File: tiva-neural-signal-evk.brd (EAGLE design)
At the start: 100 x 80 mm, 9 parts, among them IC1 TM4C123G, IC2 TLV70233, X1 USB

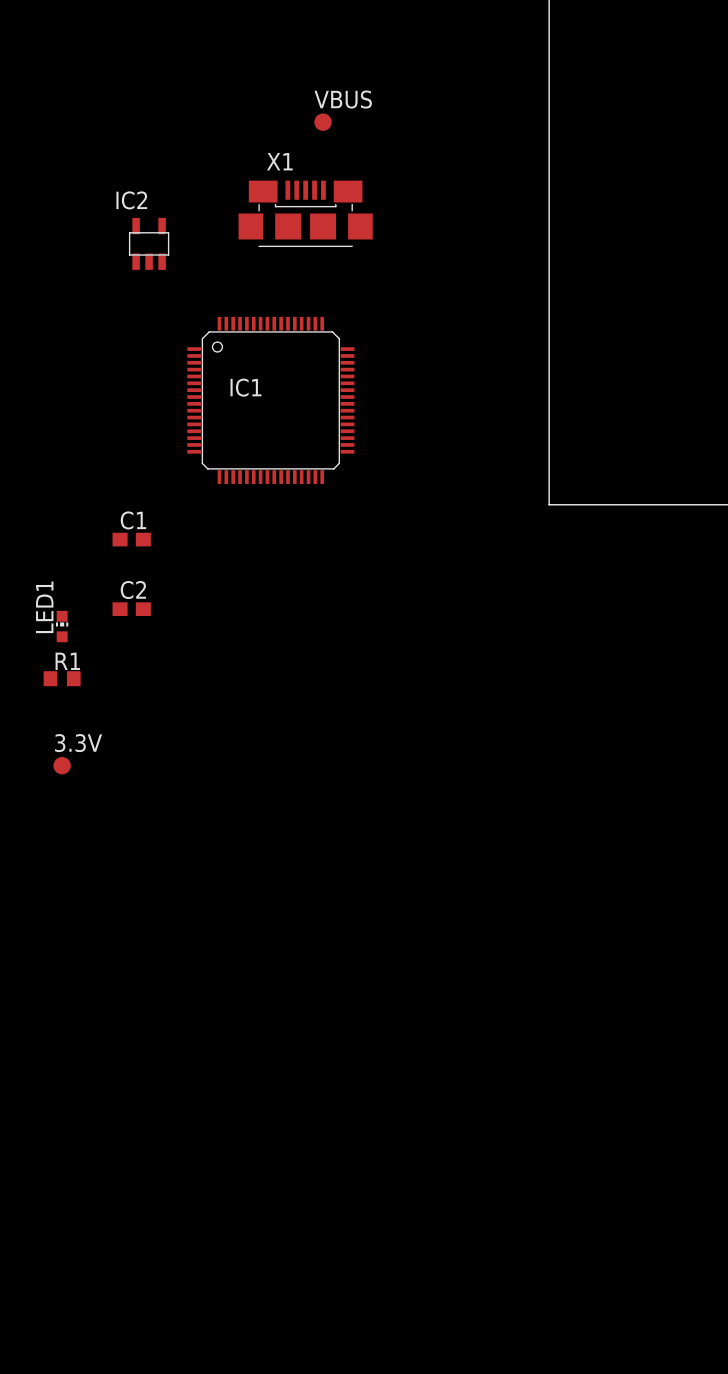
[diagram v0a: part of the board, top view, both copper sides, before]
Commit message: added MCU power circuit
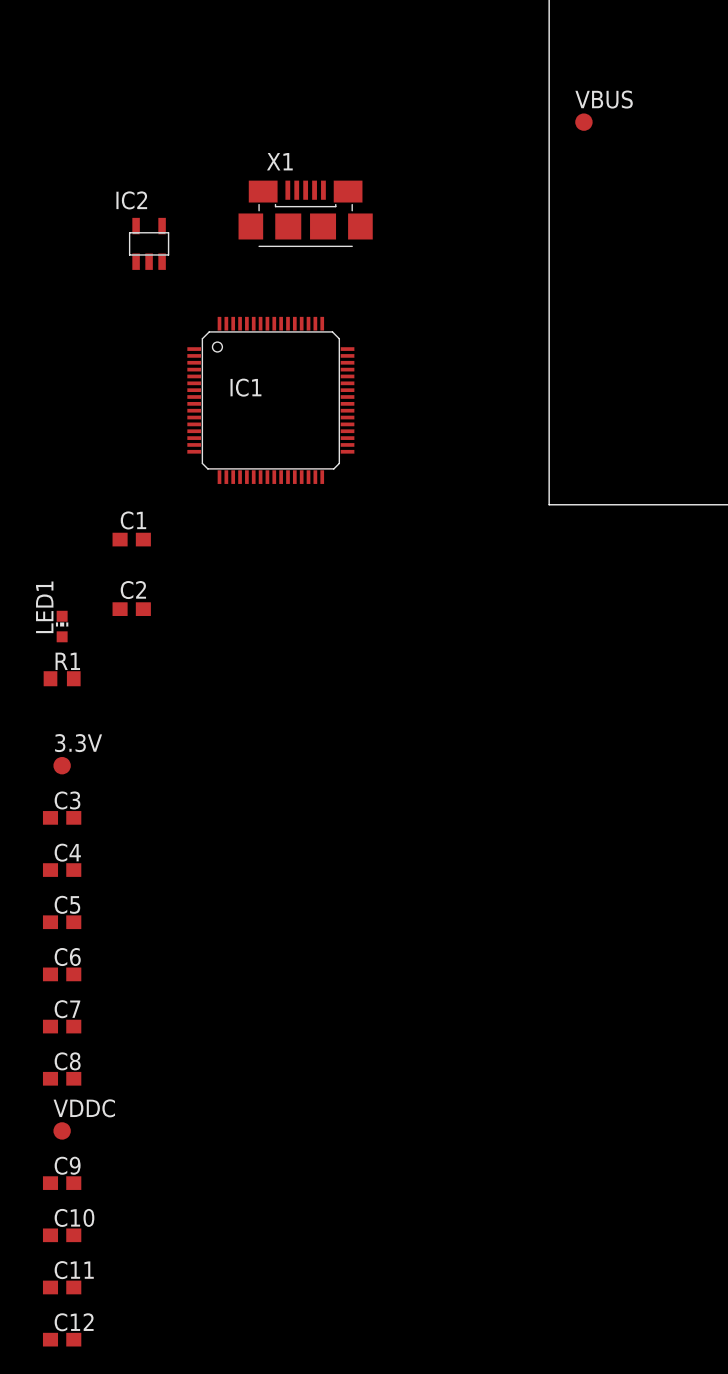
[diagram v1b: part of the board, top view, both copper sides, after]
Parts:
- added C10, C11, C12, C3, C4, C5, C6, C7, C8, C9: (no value), rcl:C0603
- added VDDC: TPB1,27, testpad:B1,27
- moved VBUS 19.1 mm to (2.54, 27.9)
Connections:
- removed net GNDA: IC1.3
- removed net VDD: IC1.11, IC1.26, IC1.42, IC1.54
- removed net VDDA: IC1.2
- removed net VDDC: IC1.25, IC1.56
- new net N$3: C3.1, C4.1, C5.1, C6.1, C7.1, C8.1, IC1.11, IC1.2, IC1.26, IC1.42, IC1.54
- new net N$4: C10.1, C11.1, C12.1, C9.1, IC1.25, IC1.56, VDDC.TP
- net GND: now also C10.2, C11.2, C12.2, C3.2, C4.2, C5.2, C6.2, C7.2, C8.2, C9.2, IC1.3
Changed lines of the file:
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@@
 <element name="X1" library="mor307" package="USB-MICROB" value="USB" x="-17.78" y="20.32"/>
 <element name="IC2" library="mor307" package="SOT23-5" value="TLV70233" x="-29.21" y="19.05"/>
-<element name="VBUS" library="testpad" package="B1,27" value="TPB1,27" x="-16.51" y="27.94">
-<attribute name="TP_SIGNAL_NAME" value="" x="0" y="0" size="1.778" layer="27" display="off"/>
+<element name="VBUS" library="testpad" package="B1,27" value="TPB1,27" x="2.54" y="27.94">
+<attribute name="TP_SIGNAL_NAME" value="" x="19.05" y="0" size="1.778" layer="27" display="off"/>
 </element>
 <element name="C1" library="resistor" package="C0603" value="1.0uF" x="-30.48" y="-2.54"/>
@@
 <attribute name="TP_SIGNAL_NAME" value="" x="-35.56" y="-19.05" size="1.778" layer="27" display="off"/>
 </element>
+<element name="C3" library="rcl" package="C0603" value="" x="-35.56" y="-22.86"/>
+<element name="C4" library="rcl" package="C0603" value="" x="-35.56" y="-26.67"/>
+<element name="C5" library="rcl" package="C0603" value="" x="-35.56" y="-30.48"/>
+<element name="C6" library="rcl" package="C0603" value="" x="-35.56" y="-34.29"/>
+<element name="C7" library="rcl" package="C0603" value="" x="-35.56" y="-38.1"/>
+<element name="C8" library="rcl" package="C0603" value="" x="-35.56" y="-41.91"/>
+<element name="VDDC" library="testpad" package="B1,27" value="TPB1,27" x="-35.56" y="-45.72">
+<attribute name="TP_SIGNAL_NAME" value="" x="-35.56" y="-45.72" size="1.778" layer="27" display="off"/>
+</element>
+<element name="C9" library="rcl" package="C0603" value="" x="-35.56" y="-49.53"/>
+<element name="C10" library="rcl" package="C0603" value="" x="-35.56" y="-53.34"/>
+<element name="C11" library="rcl" package="C0603" value="" x="-35.56" y="-57.15"/>
+<element name="C12" library="rcl" package="C0603" value="" x="-35.56" y="-60.96"/>
 </elements>
 <signals>
@@
 <contactref element="IC2" pad="2"/>
 <contactref element="LED1" pad="C"/>
+<contactref element="IC1" pad="12"/>
+<contactref element="IC1" pad="27"/>
+<contactref element="IC1" pad="39"/>
+<contactref element="IC1" pad="55"/>
+<contactref element="IC1" pad="3"/>
+<contactref element="C3" pad="2"/>
+<contactref element="C8" pad="2"/>
+<contactref element="C7" pad="2"/>
+<contactref element="C6" pad="2"/>
+<contactref element="C5" pad="2"/>
+<contactref element="C4" pad="2"/>
+<contactref element="C9" pad="2"/>
+<contactref element="C12" pad="2"/>
+<contactref element="C11" pad="2"/>
+<contactref element="C10" pad="2"/>
+<wire x1="-34.71" y1="-57.15" x2="-34.71" y2="-60.96" width="0" layer="19" extent="1-1"/>
+<wire x1="-34.71" y1="-53.34" x2="-34.71" y2="-57.15" width="0" layer="19" extent="1-1"/>
+<wire x1="-34.71" y1="-49.53" x2="-34.71" y2="-53.34" width="0" layer="19" extent="1-1"/>
+<wire x1="-34.71" y1="-41.91" x2="-34.71" y2="-49.53" width="0" layer="19" extent="1-1"/>
+<wire x1="-34.71" y1="-38.1" x2="-34.71" y2="-41.91" width="0" layer="19" extent="1-1"/>
+<wire x1="-34.71" y1="-34.29" x2="-34.71" y2="-38.1" width="0" layer="19" extent="1-1"/>
+<wire x1="-34.71" y1="-30.48" x2="-34.71" y2="-34.29" width="0" layer="19" extent="1-1"/>
+<wire x1="-34.71" y1="-26.67" x2="-34.71" y2="-30.48" width="0" layer="19" extent="1-1"/>
+<wire x1="-34.71" y1="-22.86" x2="-34.71" y2="-26.67" width="0" layer="19" extent="1-1"/>
+<wire x1="-35.56" y1="-8.14" x2="-34.71" y2="-22.86" width="0" layer="19" extent="1-1"/>
 <wire x1="-29.63" y1="-7.62" x2="-35.56" y2="-8.14" width="0" layer="19" extent="1-1"/>
 <wire x1="-29.63" y1="-2.54" x2="-29.63" y2="-7.62" width="0" layer="19" extent="1-1"/>
 <wire x1="-25.92" y1="5.87" x2="-29.63" y2="-2.54" width="0" layer="19" extent="1-1"/>
+<wire x1="-25.92" y1="10.37" x2="-25.92" y2="5.87" width="0" layer="19" extent="1-1"/>
+<wire x1="-19.57" y1="13.22" x2="-25.92" y2="10.37" width="0" layer="19" extent="1-1"/>
 <wire x1="-19.07" y1="2.02" x2="-25.92" y2="5.87" width="0" layer="19" extent="1-1"/>
 <wire x1="-14.72" y1="6.87" x2="-19.07" y2="2.02" width="0" layer="19" extent="1-1"/>
-<wire x1="-19.57" y1="13.22" x2="-14.72" y2="6.87" width="0" layer="19" extent="1-1"/>
+<wire x1="-29.21" y1="17.7499" x2="-25.92" y2="10.37" width="0" layer="19" extent="1-1"/>
 <wire x1="-16.48" y1="22.97" x2="-19.57" y2="13.22" width="0" layer="19" extent="1-1"/>
-<wire x1="-29.21" y1="17.7499" x2="-19.57" y2="13.22" width="0" layer="19" extent="1-1"/>
-</signal>
-<signal name="GNDA">
-<contactref element="IC1" pad="3"/>
-</signal>
-<signal name="VDDC">
-<contactref element="IC1" pad="56"/>
-<contactref element="IC1" pad="25"/>
-<wire x1="-20.07" y1="13.22" x2="-20.07" y2="2.02" width="0" layer="19" extent="1-1"/>
-</signal>
-<signal name="VDD">
-<contactref element="IC1" pad="54"/>
-<contactref element="IC1" pad="42"/>
-<contactref element="IC1" pad="26"/>
-<contactref element="IC1" pad="11"/>
-<wire x1="-19.57" y1="2.02" x2="-25.92" y2="6.37" width="0" layer="19" extent="1-1"/>
-<wire x1="-14.72" y1="8.37" x2="-19.57" y2="2.02" width="0" layer="19" extent="1-1"/>
-<wire x1="-19.07" y1="13.22" x2="-14.72" y2="8.37" width="0" layer="19" extent="1-1"/>
-</signal>
-<signal name="VDDA">
-<contactref element="IC1" pad="2"/>
 </signal>
 <signal name="VBAT">
@@
 <wire x1="-28.26" y1="17.7499" x2="-30.16" y2="17.7499" width="0" layer="19" extent="1-1"/>
 <wire x1="-19.08" y1="22.97" x2="-28.26" y2="17.7499" width="0" layer="19" extent="1-1"/>
-<wire x1="-16.51" y1="27.94" x2="-19.08" y2="22.97" width="0" layer="19" extent="1-1"/>
+<wire x1="2.54" y1="27.94" x2="-19.08" y2="22.97" width="0" layer="19" extent="1-1"/>
 </signal>
 <signal name="N$1">
@@
 <wire x1="-35.56" y1="-9.64" x2="-36.41" y2="-12.7" width="0" layer="19" extent="1-1"/>
 </signal>
+<signal name="N$3">
+<contactref element="IC1" pad="11"/>
+<contactref element="IC1" pad="54"/>
+<contactref element="IC1" pad="26"/>
+<contactref element="IC1" pad="42"/>
+<contactref element="IC1" pad="2"/>
+<contactref element="C8" pad="1"/>
+<contactref element="C7" pad="1"/>
+<contactref element="C6" pad="1"/>
+<contactref element="C5" pad="1"/>
+<contactref element="C4" pad="1"/>
+<contactref element="C3" pad="1"/>
+<wire x1="-36.41" y1="-38.1" x2="-36.41" y2="-41.91" width="0" layer="19" extent="1-1"/>
+<wire x1="-36.41" y1="-34.29" x2="-36.41" y2="-38.1" width="0" layer="19" extent="1-1"/>
+<wire x1="-36.41" y1="-30.48" x2="-36.41" y2="-34.29" width="0" layer="19" extent="1-1"/>
+<wire x1="-36.41" y1="-26.67" x2="-36.41" y2="-30.48" width="0" layer="19" extent="1-1"/>
+<wire x1="-36.41" y1="-22.86" x2="-36.41" y2="-26.67" width="0" layer="19" extent="1-1"/>
+<wire x1="-19.57" y1="2.02" x2="-36.41" y2="-22.86" width="0" layer="19" extent="1-1"/>
+<wire x1="-25.92" y1="6.37" x2="-19.57" y2="2.02" width="0" layer="19" extent="1-1"/>
+<wire x1="-25.92" y1="10.87" x2="-25.92" y2="6.37" width="0" layer="19" extent="1-1"/>
+<wire x1="-19.07" y1="13.22" x2="-25.92" y2="10.87" width="0" layer="19" extent="1-1"/>
+<wire x1="-14.72" y1="8.37" x2="-19.07" y2="13.22" width="0" layer="19" extent="1-1"/>
+</signal>
+<signal name="N$4">
+<contactref element="IC1" pad="25"/>
+<contactref element="VDDC" pad="TP"/>
+<contactref element="IC1" pad="56"/>
+<contactref element="C12" pad="1"/>
+<contactref element="C11" pad="1"/>
+<contactref element="C10" pad="1"/>
+<contactref element="C9" pad="1"/>
+<wire x1="-36.41" y1="-57.15" x2="-36.41" y2="-60.96" width="0" layer="19" extent="1-1"/>
+<wire x1="-36.41" y1="-53.34" x2="-36.41" y2="-57.15" width="0" layer="19" extent="1-1"/>
+<wire x1="-36.41" y1="-49.53" x2="-36.41" y2="-53.34" width="0" layer="19" extent="1-1"/>
+<wire x1="-35.56" y1="-45.72" x2="-36.41" y2="-49.53" width="0" layer="19" extent="1-1"/>
+<wire x1="-20.07" y1="2.02" x2="-35.56" y2="-45.72" width="0" layer="19" extent="1-1"/>
+<wire x1="-20.07" y1="13.22" x2="-20.07" y2="2.02" width="0" layer="19" extent="1-1"/>
+</signal>
 </signals>

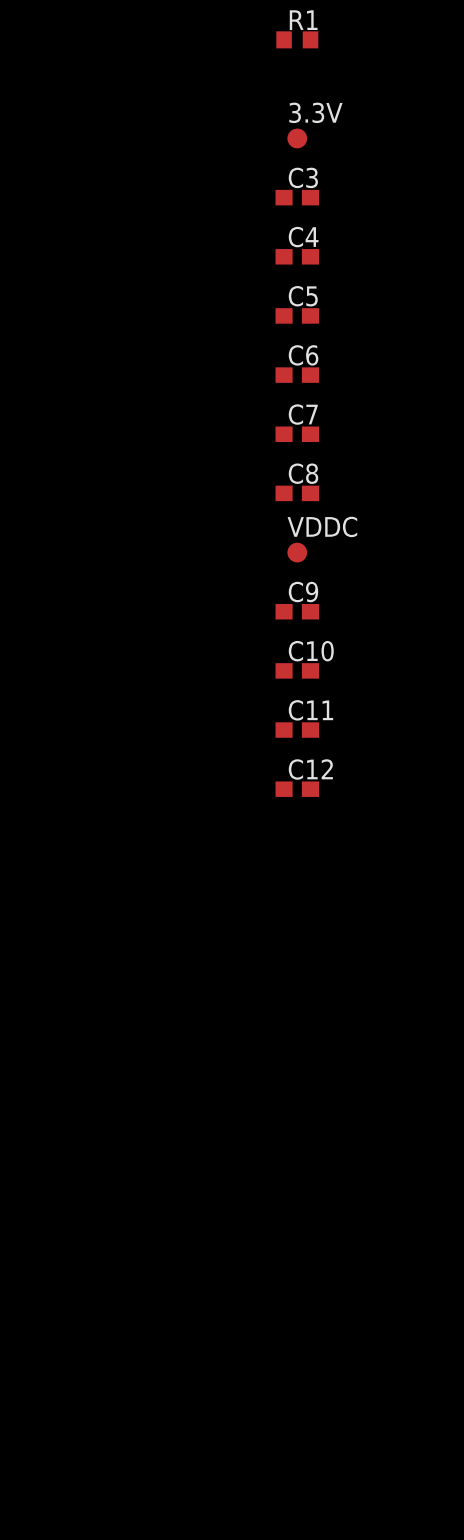
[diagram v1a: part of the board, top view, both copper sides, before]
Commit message: completed mcu control
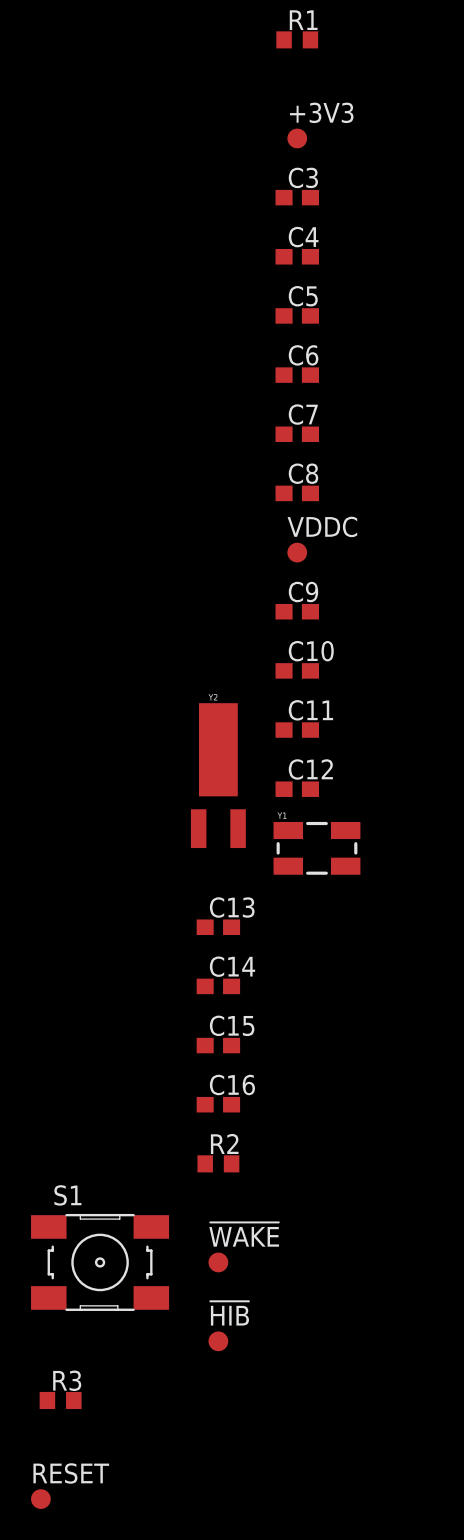
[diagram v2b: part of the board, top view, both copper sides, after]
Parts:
- added !HIB!, !WAKE!, RESET: TPB1,27, testpad:B1,27
- added C13, C14, C15, C16: (no value), rcl:C0603
- added R2, R3: 1M, rcl:R0603
- added S1: (no value), mor307:6MM_SWITCH
- added Y1: 16MHz, SparkFun-FreqCtrl:CRYSTAL-SMD-5X3
- added Y2: 32.768kHz, SparkFun-FreqCtrl:CRYSTAL-32KHZ-SMD
- renumbered 3.3V to +3V3
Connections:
- net N$4 renamed VDDC
- removed net N$1: +3V3.TP, C2.1, IC2.5, R1.2
- removed net N$3: C3.1, C4.1, C5.1, C6.1, C7.1, C8.1, IC1.11, IC1.2, IC1.26, IC1.42, IC1.54
- removed net VBAT: IC1.37
- new net !HIB!: !HIB!.TP, IC1.33
- new net !RESET!: IC1.38, R3.2, RESET.TP, S1.3, S1.4
- new net !WAKE!: !WAKE!.TP, IC1.32, R2.1
- new net +3V3: +3V3.TP, C2.1, C3.1, C4.1, C5.1, C6.1, C7.1, C8.1, IC1.11, IC1.2, IC1.26, IC1.37, IC1.42, IC1.54, IC2.5, R1.2, R2.2, R3.1
- new net N$10: C15.1, IC1.41, Y1.1
- new net N$6: C14.2, IC1.36, Y2.X2
- new net N$7: C13.2, C14.1, IC1.35
- new net N$8: C13.1, IC1.34, Y2.X1
- new net N$9: C16.1, IC1.40, Y1.3
- net GND: now also C15.2, C16.2, S1.1, S1.2

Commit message: added mcu gpio and debug buses
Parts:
- R3: value 1M -> 10k
- S1: value (none) -> RESET
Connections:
- new net PA0: IC1.17
- new net PA1: IC1.18
- new net PA2: IC1.19
- new net PA3: IC1.20
- new net PA4: IC1.21
- new net PA5: IC1.22
- new net PA6: IC1.23
- new net PA7: IC1.24
- new net PB0: IC1.45
- new net PB1: IC1.46
- new net PB2: IC1.47
- new net PB3: IC1.48
- new net PB4: IC1.58
- new net PB5: IC1.57
- new net PB6: IC1.1
- new net PB7: IC1.4
- new net PC0: IC1.52
- new net PC1: IC1.51
- new net PC2: IC1.50
- new net PC3: IC1.49
- new net PC4: IC1.16
- new net PC5: IC1.15
- new net PC6: IC1.14
- new net PC7: IC1.13
- new net PD0: IC1.61
- new net PD1: IC1.62
- new net PD2: IC1.63
- new net PD3: IC1.64
- new net PD6: IC1.53
- new net PD7: IC1.10
- new net PE0: IC1.9
- new net PE1: IC1.8
- new net PE2: IC1.7
- new net PE3: IC1.6
- new net PE4: IC1.59
- new net PE5: IC1.60
- new net PF0: IC1.28
- new net PF1: IC1.29
- new net PF2: IC1.30
- new net PF3: IC1.31
- new net PF4: IC1.5
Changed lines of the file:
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@@
 <attribute name="TP_SIGNAL_NAME" value="" x="-40.64" y="-96.52" size="1.778" layer="27" display="off"/>
 </element>
-<element name="S1" library="mor307" package="6MM_SWITCH" value="" x="-48.26" y="-91.44"/>
-<element name="R3" library="rcl" package="R0603" value="1M" x="-50.8" y="-100.33"/>
+<element name="S1" library="mor307" package="6MM_SWITCH" value="RESET" x="-48.26" y="-91.44"/>
+<element name="R3" library="rcl" package="R0603" value="10k" x="-50.8" y="-100.33"/>
 <element name="RESET" library="testpad" package="B1,27" value="TPB1,27" x="-52.07" y="-106.68">
 <attribute name="TP_SIGNAL_NAME" value="" x="-52.07" y="-106.68" size="1.778" layer="27" display="off"/>
@@
 <wire x1="-14.72" y1="6.37" x2="-44.958" y2="-93.726" width="0" layer="19" extent="1-1"/>
 </signal>
+<signal name="PC3">
+<contactref element="IC1" pad="49"/>
+</signal>
+<signal name="PA0">
+<contactref element="IC1" pad="17"/>
+</signal>
+<signal name="PA1">
+<contactref element="IC1" pad="18"/>
+</signal>
+<signal name="PC0">
+<contactref element="IC1" pad="52"/>
+</signal>
+<signal name="PC1">
+<contactref element="IC1" pad="51"/>
+</signal>
+<signal name="PC2">
+<contactref element="IC1" pad="50"/>
+</signal>
+<signal name="PA2">
+<contactref element="IC1" pad="19"/>
+</signal>
+<signal name="PA3">
+<contactref element="IC1" pad="20"/>
+</signal>
+<signal name="PA4">
+<contactref element="IC1" pad="21"/>
+</signal>
+<signal name="PA5">
+<contactref element="IC1" pad="22"/>
+</signal>
+<signal name="PA6">
+<contactref element="IC1" pad="23"/>
+</signal>
+<signal name="PA7">
+<contactref element="IC1" pad="24"/>
+</signal>
+<signal name="PC4">
+<contactref element="IC1" pad="16"/>
+</signal>
+<signal name="PC5">
+<contactref element="IC1" pad="15"/>
+</signal>
+<signal name="PC6">
+<contactref element="IC1" pad="14"/>
+</signal>
+<signal name="PC7">
+<contactref element="IC1" pad="13"/>
+</signal>
+<signal name="PE0">
+<contactref element="IC1" pad="9"/>
+</signal>
+<signal name="PE1">
+<contactref element="IC1" pad="8"/>
+</signal>
+<signal name="PE2">
+<contactref element="IC1" pad="7"/>
+</signal>
+<signal name="PE3">
+<contactref element="IC1" pad="6"/>
+</signal>
+<signal name="PE4">
+<contactref element="IC1" pad="59"/>
+</signal>
+<signal name="PE5">
+<contactref element="IC1" pad="60"/>
+</signal>
+<signal name="PB0">
+<contactref element="IC1" pad="45"/>
+</signal>
+<signal name="PB1">
+<contactref element="IC1" pad="46"/>
+</signal>
+<signal name="PB2">
+<contactref element="IC1" pad="47"/>
+</signal>
+<signal name="PB3">
+<contactref element="IC1" pad="48"/>
+</signal>
+<signal name="PB4">
+<contactref element="IC1" pad="58"/>
+</signal>
+<signal name="PB5">
+<contactref element="IC1" pad="57"/>
+</signal>
+<signal name="PB6">
+<contactref element="IC1" pad="1"/>
+</signal>
+<signal name="PB7">
+<contactref element="IC1" pad="4"/>
+</signal>
+<signal name="PD0">
+<contactref element="IC1" pad="61"/>
+</signal>
+<signal name="PD1">
+<contactref element="IC1" pad="62"/>
+</signal>
+<signal name="PD2">
+<contactref element="IC1" pad="63"/>
+</signal>
+<signal name="PD3">
+<contactref element="IC1" pad="64"/>
+</signal>
+<signal name="PD6">
+<contactref element="IC1" pad="53"/>
+</signal>
+<signal name="PD7">
+<contactref element="IC1" pad="10"/>
+</signal>
+<signal name="PF0">
+<contactref element="IC1" pad="28"/>
+</signal>
+<signal name="PF1">
+<contactref element="IC1" pad="29"/>
+</signal>
+<signal name="PF2">
+<contactref element="IC1" pad="30"/>
+</signal>
+<signal name="PF3">
+<contactref element="IC1" pad="31"/>
+</signal>
+<signal name="PF4">
+<contactref element="IC1" pad="5"/>
+</signal>
 </signals>
